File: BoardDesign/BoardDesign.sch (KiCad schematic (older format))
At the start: 9 parts, among them U1 CC56-12CGKWA, U2 74HC595

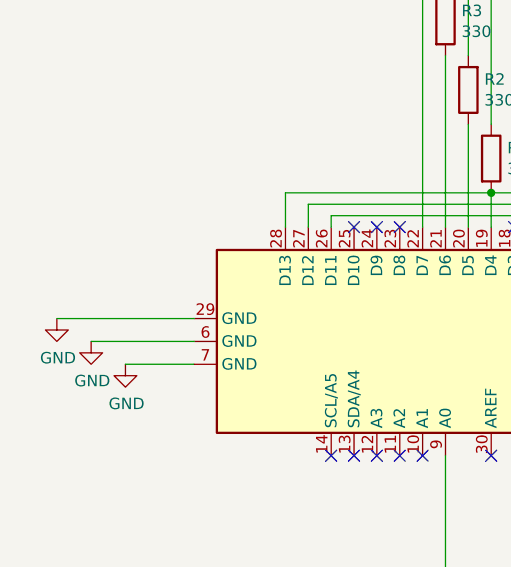
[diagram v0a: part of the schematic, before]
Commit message: Fixed the board design to implement proper GND tags.
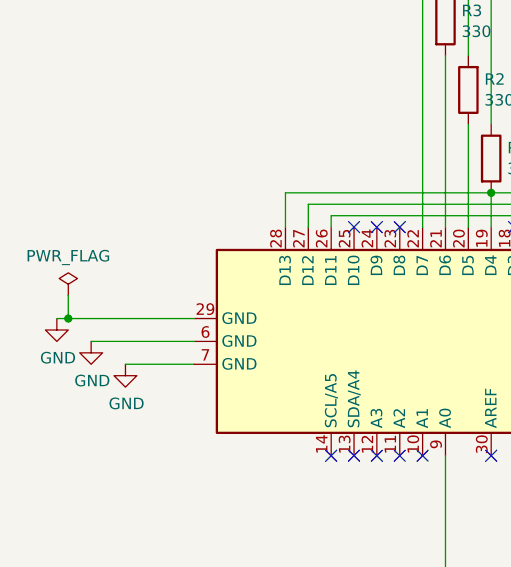
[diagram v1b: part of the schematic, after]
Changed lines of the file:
@@
 	4650 4300 4200 4300
 Wire Wire Line
-	4650 4200 4050 4200
+	4650 4200 4100 4200
+$Comp
+L power:PWR_FLAG #FLG0101
+U 1 1 5FC48752
+P 4100 4100
+F 0 "#FLG0101" H 4100 4175 50  0001 C CNN
+F 1 "PWR_FLAG" H 4100 4273 50  0000 C CNN
+F 2 "" H 4100 4100 50  0001 C CNN
+F 3 "~" H 4100 4100 50  0001 C CNN
+	1    4100 4100
+	1    0    0    -1
+$EndComp
+Wire Wire Line
+	4100 4100 4100 4200
+Connection ~ 4100 4200
+Wire Wire Line
+	4100 4200 4050 4200
 $EndSCHEMATC

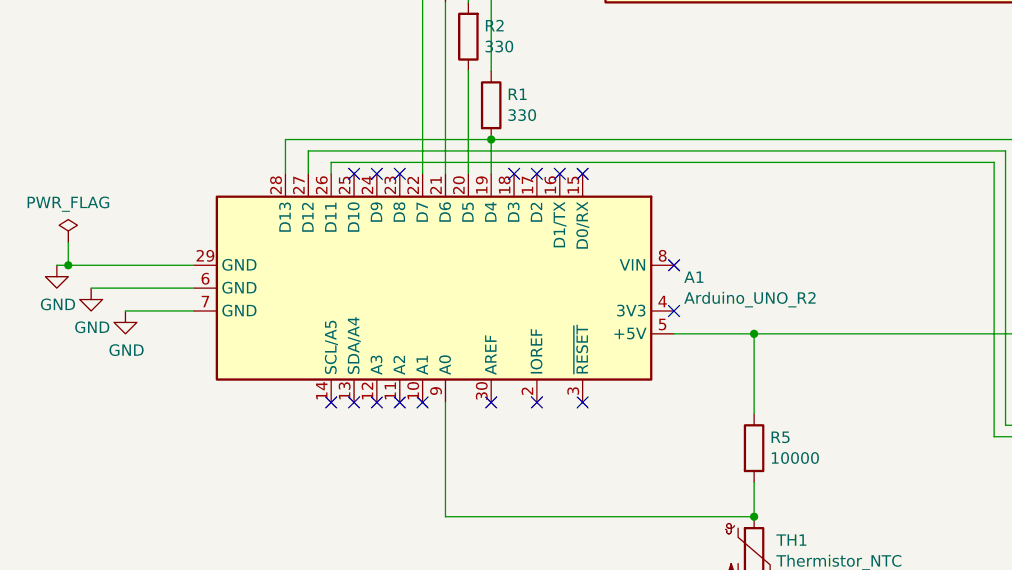
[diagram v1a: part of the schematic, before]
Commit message: Finished the layout for the first board.
Added files needed to have a board fabricated.
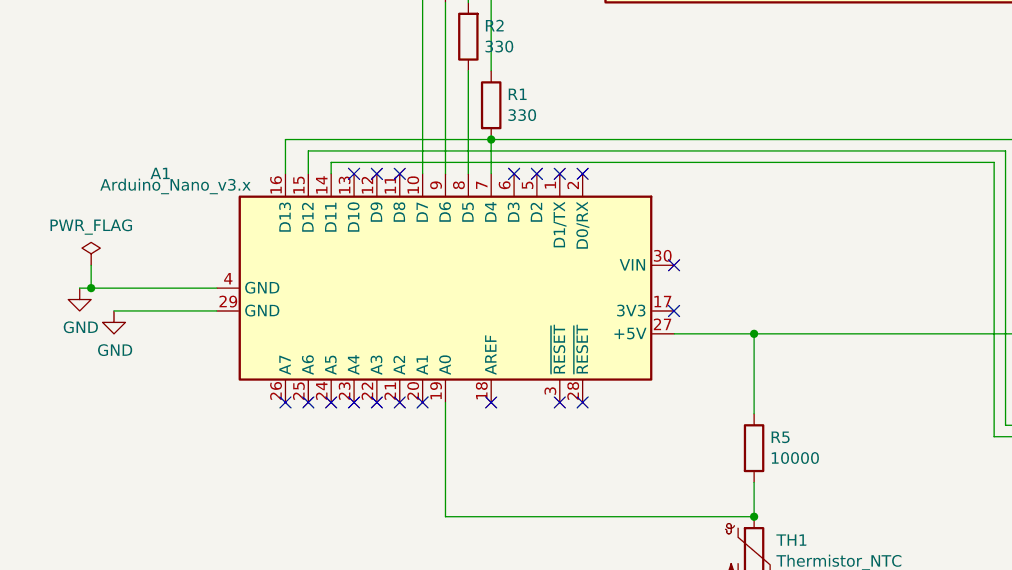
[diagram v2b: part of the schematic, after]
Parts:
- removed A1: Arduino_UNO_R2, Module:Arduino_UNO_R2, symbol MCU_Module:Arduino_UNO_R2
- added A1: Arduino_Nano_v3.x, Module:Arduino_Nano_WithMountingHoles, symbol MCU_Module:Arduino_Nano_v3.x
- R1, R2, R3, R4, R5, TH1: footprint (none) -> Resistor_SMD:R_0805_2012Metric
- U1: footprint Display_7Segment:CA56-12CGKWA -> CircuitBoard:HKL-8041-AB
- U2: footprint (none) -> Package_DIP:DIP-16_W7.62mm_LongPads
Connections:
- net GND: now also A1.29 (GND), A1.4 (GND)
- net at R1.2, U2.14 (SER): now also A1.16 (D13), A1.7 (D4)
- net at R2.1: now also A1.8 (D5)
- net at R3.2: now also A1.9 (D6)
- net at R4.2: now also A1.10 (D7)
- net at U2.11 (SRCLK): now also A1.14 (D11)
- net at U2.12 (RCLK): now also A1.15 (D12)
- net at R5.1, U2.10 (~SRCLR), U2.16 (VCC): now also A1.27 (+5V)
- net at R5.2, TH1.1: now also A1.19 (A0)
- no-connect marks 18 -> 20
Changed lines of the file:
@@
 $EndDescr
-$Comp
-L MCU_Module:Arduino_UNO_R2 A1
-U 1 1 5FC338F6
-P 5750 4300
-F 0 "A1" V 5704 5344 50  0000 L CNN
-F 1 "Arduino_UNO_R2" V 5795 5344 50  0000 L CNN
-F 2 "Module:Arduino_UNO_R2" H 5750 4300 50  0001 C CIN
-F 3 "https://www.arduino.cc/en/Main/arduinoBoardUno" H 5750 4300 50  0001 C CNN
-	1    5750 4300
-	0    1    1    0
-$EndComp
 $Comp
 L Device:R R4
@@
 F 0 "R4" H 5720 2646 50  0000 L CNN
 F 1 "330" H 5720 2555 50  0000 L CNN
-F 2 "" V 5580 2600 50  0001 C CNN
+F 2 "Resistor_SMD:R_0805_2012Metric" V 5580 2600 50  0001 C CNN
 F 3 "~" H 5650 2600 50  0001 C CNN
 	1    5650 2600
@@
 F 0 "R3" H 5820 2946 50  0000 L CNN
 F 1 "330" H 5820 2855 50  0000 L CNN
-F 2 "" V 5680 2900 50  0001 C CNN
+F 2 "Resistor_SMD:R_0805_2012Metric" V 5680 2900 50  0001 C CNN
 F 3 "~" H 5750 2900 50  0001 C CNN
 	1    5750 2900
@@
 F 0 "R2" H 5780 3154 50  0000 R CNN
 F 1 "330" H 5780 3245 50  0000 R CNN
-F 2 "" V 5780 3200 50  0001 C CNN
+F 2 "Resistor_SMD:R_0805_2012Metric" V 5780 3200 50  0001 C CNN
 F 3 "~" H 5850 3200 50  0001 C CNN
 	1    5850 3200
@@
 F 0 "R1" H 6020 3546 50  0000 L CNN
 F 1 "330" H 6020 3455 50  0000 L CNN
-F 2 "" V 5880 3500 50  0001 C CNN
+F 2 "Resistor_SMD:R_0805_2012Metric" V 5880 3500 50  0001 C CNN
 F 3 "~" H 5950 3500 50  0001 C CNN
 	1    5950 3500
@@
 F 0 "U1" H 7450 1883 50  0000 C CNN
 F 1 "CC56-12CGKWA" H 7450 1974 50  0000 C CNN
-F 2 "Display_7Segment:CA56-12CGKWA" H 7450 1950 50  0001 C CNN
+F 2 "CircuitBoard:HKL-8041-AB" H 7450 1950 50  0001 C CNN
 F 3 "http://www.kingbright.com/attachments/file/psearch/000/00/00/CC56-12CGKWA(Ver.8A).pdf" H 7020 2580 50  0001 C CNN
 	1    7450 2550
@@
 F 0 "U2" V 9346 3556 50  0000 R CNN
 F 1 "74HC595" V 9255 3556 50  0000 R CNN
-F 2 "" H 9300 4300 50  0001 C CNN
+F 2 "Package_DIP:DIP-16_W7.62mm_LongPads" H 9300 4300 50  0001 C CNN
 F 3 "http://www.ti.com/lit/ds/symlink/sn74hc595.pdf" H 9300 4300 50  0001 C CNN
 	1    9300 4300
@@
 NoConn ~ 5250 4800
 NoConn ~ 5950 4800
-NoConn ~ 6150 4800
 NoConn ~ 6350 4800
 NoConn ~ 6750 4400
@@
 F 0 "R5" H 7170 5046 50  0000 L CNN
 F 1 "10000" H 7170 4955 50  0000 L CNN
-F 2 "" V 7030 5000 50  0001 C CNN
+F 2 "Resistor_SMD:R_0805_2012Metric" V 7030 5000 50  0001 C CNN
 F 3 "~" H 7100 5000 50  0001 C CNN
 	1    7100 5000
@@
 F 0 "TH1" H 7198 5496 50  0000 L CNN
 F 1 "Thermistor_NTC" H 7198 5405 50  0000 L CNN
-F 2 "" H 7100 5500 50  0001 C CNN
+F 2 "Resistor_SMD:R_0805_2012Metric" H 7100 5500 50  0001 C CNN
 F 3 "~" H 7100 5500 50  0001 C CNN
 	1    7100 5450
@@
 L power:GND #PWR0101
 U 1 1 5FCA7732
-P 4050 4200
-F 0 "#PWR0101" H 4050 3950 50  0001 C CNN
-F 1 "GND" H 4055 4027 50  0000 C CNN
-F 2 "" H 4050 4200 50  0001 C CNN
-F 3 "" H 4050 4200 50  0001 C CNN
-	1    4050 4200
+P 4150 4300
+F 0 "#PWR0101" H 4150 4050 50  0001 C CNN
+F 1 "GND" H 4155 4127 50  0000 C CNN
+F 2 "" H 4150 4300 50  0001 C CNN
+F 3 "" H 4150 4300 50  0001 C CNN
+	1    4150 4300
 	1    0    0    -1
 $EndComp
@@
 L power:GND #PWR0102
 U 1 1 5FCA7CF9
-P 4200 4300
-F 0 "#PWR0102" H 4200 4050 50  0001 C CNN
-F 1 "GND" H 4205 4127 50  0000 C CNN
-F 2 "" H 4200 4300 50  0001 C CNN
-F 3 "" H 4200 4300 50  0001 C CNN
-	1    4200 4300
-	1    0    0    -1
-$EndComp
-$Comp
-L power:GND #PWR0103
-U 1 1 5FCA817D
-P 4350 4400
-F 0 "#PWR0103" H 4350 4150 50  0001 C CNN
-F 1 "GND" H 4355 4227 50  0000 C CNN
-F 2 "" H 4350 4400 50  0001 C CNN
-F 3 "" H 4350 4400 50  0001 C CNN
-	1    4350 4400
+P 4300 4400
+F 0 "#PWR0102" H 4300 4150 50  0001 C CNN
+F 1 "GND" H 4305 4227 50  0000 C CNN
+F 2 "" H 4300 4400 50  0001 C CNN
+F 3 "" H 4300 4400 50  0001 C CNN
+	1    4300 4400
 	1    0    0    -1
 $EndComp
@@
 	7100 5600 7100 5700
 Wire Wire Line
-	4650 4400 4350 4400
-Wire Wire Line
-	4650 4300 4200 4300
-Wire Wire Line
-	4650 4200 4100 4200
+	4750 4400 4300 4400
+Wire Wire Line
+	4750 4300 4200 4300
 $Comp
 L power:PWR_FLAG #FLG0101
 U 1 1 5FC48752
-P 4100 4100
-F 0 "#FLG0101" H 4100 4175 50  0001 C CNN
-F 1 "PWR_FLAG" H 4100 4273 50  0000 C CNN
-F 2 "" H 4100 4100 50  0001 C CNN
-F 3 "~" H 4100 4100 50  0001 C CNN
-	1    4100 4100
-	1    0    0    -1
-$EndComp
-Wire Wire Line
-	4100 4100 4100 4200
-Connection ~ 4100 4200
-Wire Wire Line
-	4100 4200 4050 4200
+P 4200 4200
+F 0 "#FLG0101" H 4200 4275 50  0001 C CNN
+F 1 "PWR_FLAG" H 4200 4373 50  0000 C CNN
+F 2 "" H 4200 4200 50  0001 C CNN
+F 3 "~" H 4200 4200 50  0001 C CNN
+	1    4200 4200
+	1    0    0    -1
+$EndComp
+Wire Wire Line
+	4200 4200 4200 4300
+Connection ~ 4200 4300
+Wire Wire Line
+	4200 4300 4150 4300
+$Comp
+L MCU_Module:Arduino_Nano_v3.x A1
+U 1 1 5FC75C97
+P 5750 4300
+F 0 "A1" V 5250 3100 50  0000 R CNN
+F 1 "Arduino_Nano_v3.x" V 5300 3450 50  0000 R CNN
+F 2 "Module:Arduino_Nano_WithMountingHoles" H 5750 4300 50  0001 C CIN
+F 3 "http://www.mouser.com/pdfdocs/Gravitech_Arduino_Nano3_0.pdf" H 5750 4300 50  0001 C CNN
+	1    5750 4300
+	0    1    1    0
+$EndComp
+NoConn ~ 6250 4800
+NoConn ~ 5150 4800
+NoConn ~ 5050 4800
 $EndSCHEMATC

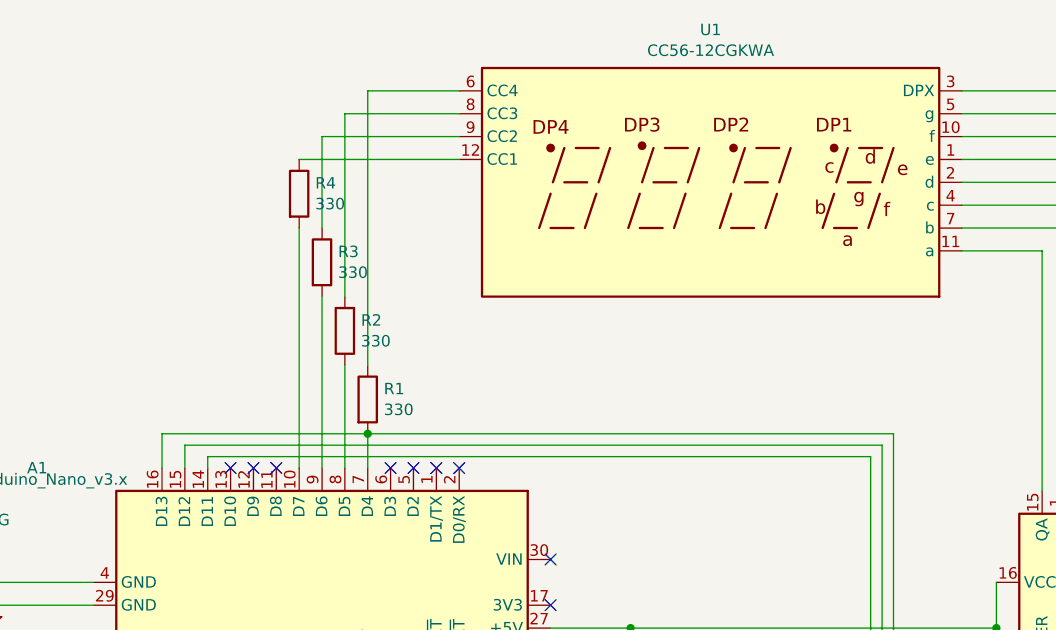
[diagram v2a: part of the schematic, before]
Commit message: Fixed Issue with R4 Trace
Had an accidental junction in the schematic.
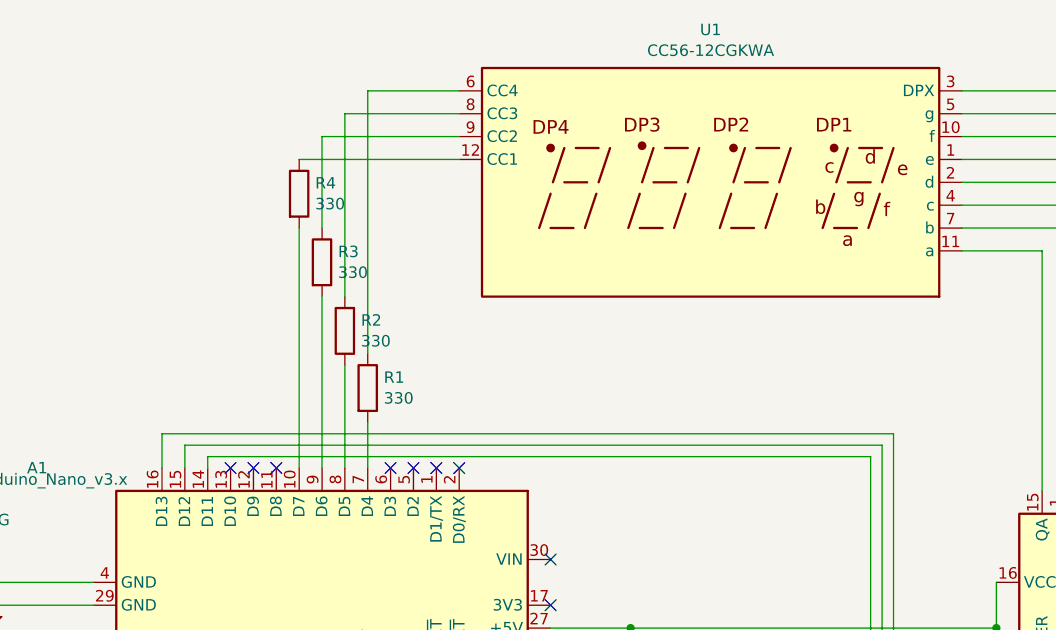
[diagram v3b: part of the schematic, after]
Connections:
- net at A1.7 (D4), R1.2: no longer A1.16 (D13), U2.14 (SER)
- new net: A1.16 (D13), U2.14 (SER)
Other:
- moved on the sheet: R1
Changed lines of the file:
@@
 L Device:R R1
 U 1 1 5FC39072
-P 5950 3500
-F 0 "R1" H 6020 3546 50  0000 L CNN
-F 1 "330" H 6020 3455 50  0000 L CNN
-F 2 "Resistor_SMD:R_0805_2012Metric" V 5880 3500 50  0001 C CNN
-F 3 "~" H 5950 3500 50  0001 C CNN
-	1    5950 3500
-	1    0    0    -1
-$EndComp
-Wire Wire Line
-	5950 3800 5950 3650
+P 5950 3450
+F 0 "R1" H 6020 3496 50  0000 L CNN
+F 1 "330" H 6020 3405 50  0000 L CNN
+F 2 "Resistor_SMD:R_0805_2012Metric" V 5880 3450 50  0001 C CNN
+F 3 "~" H 5950 3450 50  0001 C CNN
+	1    5950 3450
+	1    0    0    -1
+$EndComp
 $Comp
 L Display_Character:CC56-12CGKWA U1
@@
 	5850 2250 6350 2250
 Wire Wire Line
-	5950 3350 5950 2150
-Wire Wire Line
 	5950 2150 6350 2150
 Wire Wire Line
@@
 Wire Wire Line
 	9600 2150 8550 2150
-Wire Wire Line
-	5050 3800 5050 3650
-Wire Wire Line
-	5050 3650 5950 3650
-Wire Wire Line
-	8250 3650 8250 4850
-Wire Wire Line
-	8250 4850 8900 4850
-Wire Wire Line
-	8900 4850 8900 4700
-Connection ~ 5950 3650
-Wire Wire Line
-	5950 3650 8250 3650
 Wire Wire Line
 	5150 3800 5150 3700
@@
 NoConn ~ 5150 4800
 NoConn ~ 5050 4800
+Wire Wire Line
+	8900 4850 8900 4700
+Wire Wire Line
+	8250 4850 8900 4850
+Wire Wire Line
+	8250 3650 8250 4850
+Wire Wire Line
+	5050 3800 5050 3650
+Wire Wire Line
+	5050 3650 8250 3650
+Wire Wire Line
+	5950 3800 5950 3600
+Wire Wire Line
+	5950 3300 5950 2150
 $EndSCHEMATC

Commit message: Finished the V2 Design
Corrected the general issues with the board. Notably, fixed the
disconnected traces to the 330 Ohm resistors, swapped the positions of
the thermistor and loading resistor, added M2 screw holes and moved pin
13 to pin 10 for the coms to the shift register.
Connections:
- net GND: now also R5.2; no longer TH1.2
- net at A1.27 (+5V), U2.10 (~SRCLR), U2.16 (VCC): now also TH1.1; no longer R5.1
- net at U2.14 (SER): now also A1.13 (D10); no longer A1.16 (D13)
- new net: A1.19 (A0), R5.1, TH1.2
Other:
- moved on the sheet: R5, TH1
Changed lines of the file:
@@
 L Device:R R5
 U 1 1 5FC67A15
-P 7100 5000
-F 0 "R5" H 7170 5046 50  0000 L CNN
-F 1 "10000" H 7170 4955 50  0000 L CNN
-F 2 "Resistor_SMD:R_0805_2012Metric" V 7030 5000 50  0001 C CNN
-F 3 "~" H 7100 5000 50  0001 C CNN
-	1    7100 5000
+P 7100 5450
+F 0 "R5" H 7170 5496 50  0000 L CNN
+F 1 "10000" H 7170 5405 50  0000 L CNN
+F 2 "Resistor_SMD:R_0805_2012Metric" V 7030 5450 50  0001 C CNN
+F 3 "~" H 7100 5450 50  0001 C CNN
+	1    7100 5450
 	1    0    0    -1
 $EndComp
@@
 L Device:Thermistor_NTC TH1
 U 1 1 5FC68995
-P 7100 5450
-F 0 "TH1" H 7198 5496 50  0000 L CNN
-F 1 "Thermistor_NTC" H 7198 5405 50  0000 L CNN
-F 2 "Resistor_SMD:R_0805_2012Metric" H 7100 5500 50  0001 C CNN
-F 3 "~" H 7100 5500 50  0001 C CNN
-	1    7100 5450
+P 7100 5000
+F 0 "TH1" H 7198 5046 50  0000 L CNN
+F 1 "Thermistor_NTC" H 7198 4955 50  0000 L CNN
+F 2 "Resistor_SMD:R_0805_2012Metric" H 7100 5050 50  0001 C CNN
+F 3 "~" H 7100 5050 50  0001 C CNN
+	1    7100 5000
 	1    0    0    -1
 $EndComp
@@
 Wire Wire Line
 	5750 5300 5750 4800
-Connection ~ 7100 5300
 NoConn ~ 6050 3800
 NoConn ~ 6150 3800
@@
 NoConn ~ 5550 3800
 NoConn ~ 5450 3800
-NoConn ~ 5350 3800
 $Comp
 L power:GND #PWR0101
@@
 	8250 3650 8250 4850
 Wire Wire Line
-	5050 3800 5050 3650
-Wire Wire Line
-	5050 3650 8250 3650
-Wire Wire Line
 	5950 3800 5950 3600
 Wire Wire Line
 	5950 3300 5950 2150
+Wire Wire Line
+	5350 3800 5350 3650
+Wire Wire Line
+	5350 3650 8250 3650
+NoConn ~ 5050 3800
+Connection ~ 7100 5300
 $EndSCHEMATC
